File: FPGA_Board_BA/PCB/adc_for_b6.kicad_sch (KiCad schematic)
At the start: 17 parts, among them U1 LTC2320-16_CMOS

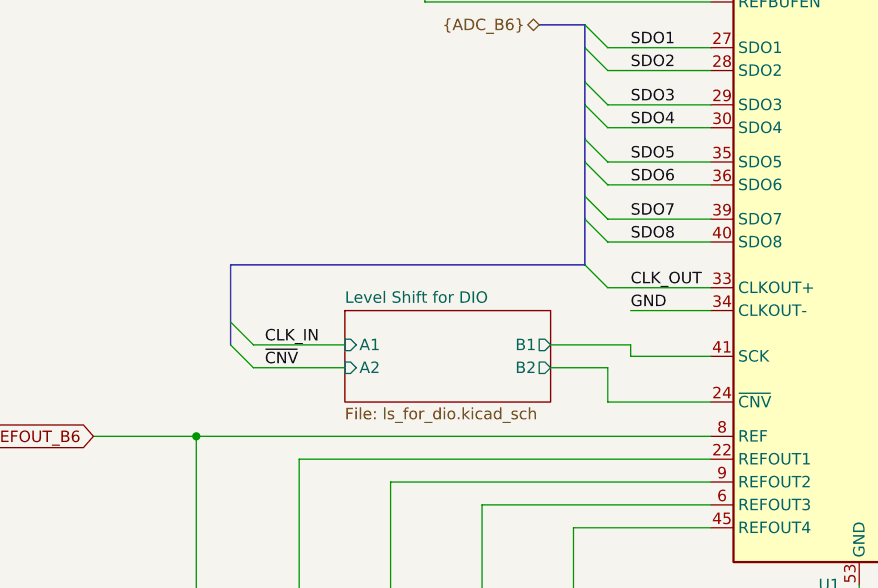
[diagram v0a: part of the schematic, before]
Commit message: optimised pinout in schematic + added level shifter for CLKOUT + got forward with layout
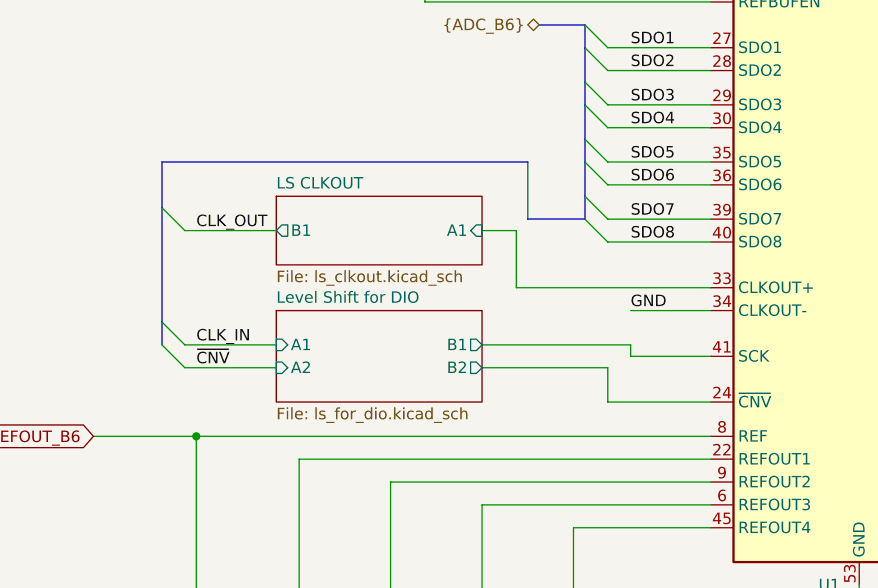
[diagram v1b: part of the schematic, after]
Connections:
- net CLK_OUT: no longer U1.33 (CLKOUT+)
- new net LS CLKOUT/A1: U1.33 (CLKOUT+)
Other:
- added sheet LS CLKOUT (ls_clkout.kicad_sch)
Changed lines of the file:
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@@
 	)
 	(bus_entry
-		(at 102.87 102.87)
+		(at 95.25 102.87)
 		(size -2.54 -2.54)
 		(stroke
@@
 	)
 	(bus_entry
-		(at 102.87 100.33)
+		(at 95.25 100.33)
 		(size -2.54 -2.54)
 		(stroke
@@
 	)
 	(bus_entry
-		(at 142.24 93.98)
+		(at 95.25 87.63)
 		(size -2.54 -2.54)
 		(stroke
@@
 		)
 	)
+	(bus
+		(pts
+			(xy 133.35 80.01) (xy 92.71 80.01)
+		)
+		(stroke
+			(width 0)
+			(type default)
+		)
+	)
 	(wire
 		(pts
@@
 	(wire
 		(pts
-			(xy 102.87 100.33) (xy 113.03 100.33)
+			(xy 95.25 100.33) (xy 105.41 100.33)
 		)
 		(stroke
@@
 	(wire
 		(pts
-			(xy 135.89 102.87) (xy 142.24 102.87)
+			(xy 128.27 102.87) (xy 142.24 102.87)
 		)
 		(stroke
@@
 	(bus
 		(pts
-			(xy 100.33 91.44) (xy 139.7 91.44)
-		)
-		(stroke
-			(width 0)
-			(type default)
-		)
-	)
-	(bus
-		(pts
 			(xy 251.46 91.44) (xy 251.46 78.74)
 		)
@@
 		)
 	)
+	(bus
+		(pts
+			(xy 133.35 86.36) (xy 133.35 80.01)
+		)
+		(stroke
+			(width 0)
+			(type default)
+		)
+	)
 	(wire
 		(pts
@@
 	(wire
 		(pts
+			(xy 128.27 87.63) (xy 132.08 87.63)
+		)
+		(stroke
+			(width 0)
+			(type default)
+		)
+	)
+	(wire
+		(pts
 			(xy 96.52 128.27) (xy 96.52 110.49)
 		)
@@
 	(bus
 		(pts
+			(xy 92.71 80.01) (xy 92.71 85.09)
+		)
+		(stroke
+			(width 0)
+			(type default)
+		)
+	)
+	(bus
+		(pts
 			(xy 251.46 104.14) (xy 251.46 116.84)
 		)
@@
 	(wire
 		(pts
+			(xy 132.08 87.63) (xy 132.08 93.98)
+		)
+		(stroke
+			(width 0)
+			(type default)
+		)
+	)
+	(wire
+		(pts
 			(xy 184.15 109.22) (xy 200.66 109.22)
 		)
@@
 		)
 	)
+	(bus
+		(pts
+			(xy 133.35 86.36) (xy 139.7 86.36)
+		)
+		(stroke
+			(width 0)
+			(type default)
+		)
+	)
 	(wire
 		(pts
@@
 		)
 	)
+	(bus
+		(pts
+			(xy 92.71 85.09) (xy 92.71 97.79)
+		)
+		(stroke
+			(width 0)
+			(type default)
+		)
+	)
 	(wire
 		(pts
@@
 	(wire
 		(pts
-			(xy 142.24 93.98) (xy 153.67 93.98)
+			(xy 95.25 87.63) (xy 105.41 87.63)
 		)
 		(stroke
@@
 		)
 	)
-	(bus
-		(pts
-			(xy 139.7 91.44) (xy 139.7 86.36)
-		)
-		(stroke
-			(width 0)
-			(type default)
-		)
-	)
 	(wire
 		(pts
@@
 	(wire
 		(pts
-			(xy 102.87 102.87) (xy 113.03 102.87)
+			(xy 95.25 102.87) (xy 105.41 102.87)
 		)
 		(stroke
@@
 	(wire
 		(pts
-			(xy 135.89 100.33) (xy 144.78 100.33)
+			(xy 128.27 100.33) (xy 144.78 100.33)
 		)
 		(stroke
@@
 	(bus
 		(pts
-			(xy 100.33 97.79) (xy 100.33 100.33)
+			(xy 92.71 97.79) (xy 92.71 100.33)
 		)
 		(stroke
@@
 	(wire
 		(pts
-			(xy 142.24 106.68) (xy 153.67 106.68)
+			(xy 132.08 93.98) (xy 153.67 93.98)
 		)
 		(stroke
@@
 	(wire
 		(pts
-			(xy 190.5 132.08) (xy 190.5 133.35)
+			(xy 142.24 106.68) (xy 153.67 106.68)
 		)
 		(stroke
@@
 	(wire
 		(pts
-			(xy 198.12 57.15) (xy 198.12 71.12)
+			(xy 190.5 132.08) (xy 190.5 133.35)
 		)
 		(stroke
@@
 	(wire
 		(pts
-			(xy 49.53 157.48) (xy 49.53 161.29)
+			(xy 198.12 57.15) (xy 198.12 71.12)
 		)
 		(stroke
@@
 	(wire
 		(pts
-			(xy 205.74 101.6) (xy 205.74 107.95)
+			(xy 49.53 157.48) (xy 49.53 161.29)
 		)
 		(stroke
@@
 		)
 	)
-	(bus
+	(wire
 		(pts
-			(xy 100.33 91.44) (xy 100.33 97.79)
+			(xy 205.74 101.6) (xy 205.74 107.95)
 		)
 		(stroke
@@
 	)
 	(label "CLK_IN"
-		(at 104.14 100.33 0)
+		(at 96.52 100.33 0)
 		(effects
 			(font
@@
 	)
 	(label "CLK_OUT"
-		(at 144.78 93.98 0)
+		(at 96.52 87.63 0)
 		(effects
 			(font
@@
 	)
 	(label "~{CNV}"
-		(at 104.14 102.87 0)
+		(at 96.52 102.87 0)
 		(effects
 			(font
@@
 	)
 	(sheet
+		(at 105.41 83.82)
+		(size 22.86 7.62)
+		(exclude_from_sim no)
+		(in_bom yes)
+		(on_board yes)
+		(dnp no)
+		(fields_autoplaced yes)
+		(stroke
+			(width 0.1524)
+			(type solid)
+		)
+		(fill
+			(color 0 0 0 0.0000)
+		)
+		(property "Sheetname" "LS CLKOUT"
+			(at 105.41 83.1084 0)
+			(effects
+				(font
+					(size 1.27 1.27)
+				)
+				(justify left bottom)
+			)
+		)
+		(property "Sheetfile" "ls_clkout.kicad_sch"
+			(at 105.41 92.0246 0)
+			(effects
+				(font
+					(size 1.27 1.27)
+				)
+				(justify left top)
+			)
+		)
+		(pin "A1" input
+			(at 128.27 87.63 0)
+			(effects
+				(font
+					(size 1.27 1.27)
+				)
+				(justify right)
+			)
+		)
+		(pin "B1" output
+			(at 105.41 87.63 180)
+			(effects
+				(font
+					(size 1.27 1.27)
+				)
+				(justify left)
+			)
+		)
+		(instances
+			(project "FPGA_Board_BA"
+				(path "/fd7503bc-e7fc-4766-b224-3d1c3d7de5ff/b651456b-f82d-416a-adc2-766f971f7bfa"
+					(page "8")
+				)
+			)
+		)
+	)
+	(sheet
 		(at 215.9 90.17)
 		(size 25.4 7.62)
@@
 	)
 	(sheet
-		(at 113.03 96.52)
+		(at 105.41 96.52)
 		(size 22.86 10.16)
 		(exclude_from_sim no)
@@
 		)
 		(property "Sheetname" "Level Shift for DIO"
-			(at 113.03 95.8084 0)
+			(at 105.41 95.8084 0)
 			(effects
 				(font
@@
 		)
 		(property "Sheetfile" "ls_for_dio.kicad_sch"
-			(at 113.03 107.2646 0)
+			(at 105.41 107.2646 0)
 			(effects
 				(font
@@
 		)
 		(pin "A1" input
-			(at 113.03 100.33 180)
+			(at 105.41 100.33 180)
 			(effects
 				(font
@@
 		)
 		(pin "A2" input
-			(at 113.03 102.87 180)
+			(at 105.41 102.87 180)
 			(effects
 				(font
@@
 		)
 		(pin "B1" output
-			(at 135.89 100.33 0)
+			(at 128.27 100.33 0)
 			(effects
 				(font
@@
 		)
 		(pin "B2" output
-			(at 135.89 102.87 0)
+			(at 128.27 102.87 0)
 			(effects
 				(font

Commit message: Nach meeting mit Leo
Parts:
- removed C12, C13, C14, C15: 10u_1210, WLIB_Capacitor:C_1210, symbol WLIB_C:10u_1210
- added C12, C13, C14, C15: 10u_0603, Capacitor_SMD:C_0603_1608Metric, symbol MYLIB_Misc:10u_0603
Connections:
- net GND: now also C12.1, C13.1, C14.1, C15.1
- net at U1.22 (REFOUT1): now also C12.2
- net at U1.45 (REFOUT4): now also C15.2
- net at U1.6 (REFOUT3): now also C14.2
- net at U1.9 (REFOUT2): now also C13.2
